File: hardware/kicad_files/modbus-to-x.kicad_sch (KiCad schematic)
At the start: 67 parts, among them IC1 ESP32-WROOM-32D_M113DH2800PH3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, J1 PWR, J2 UART, J3 Screw_Terminal_3.5mm_2, SW1 1825910-7, SW2 1825910-7, U1 AMS1117-3.3, U3 MAX3485, U5 AT24CS64-XHM, U6 AT24CS64-XHM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

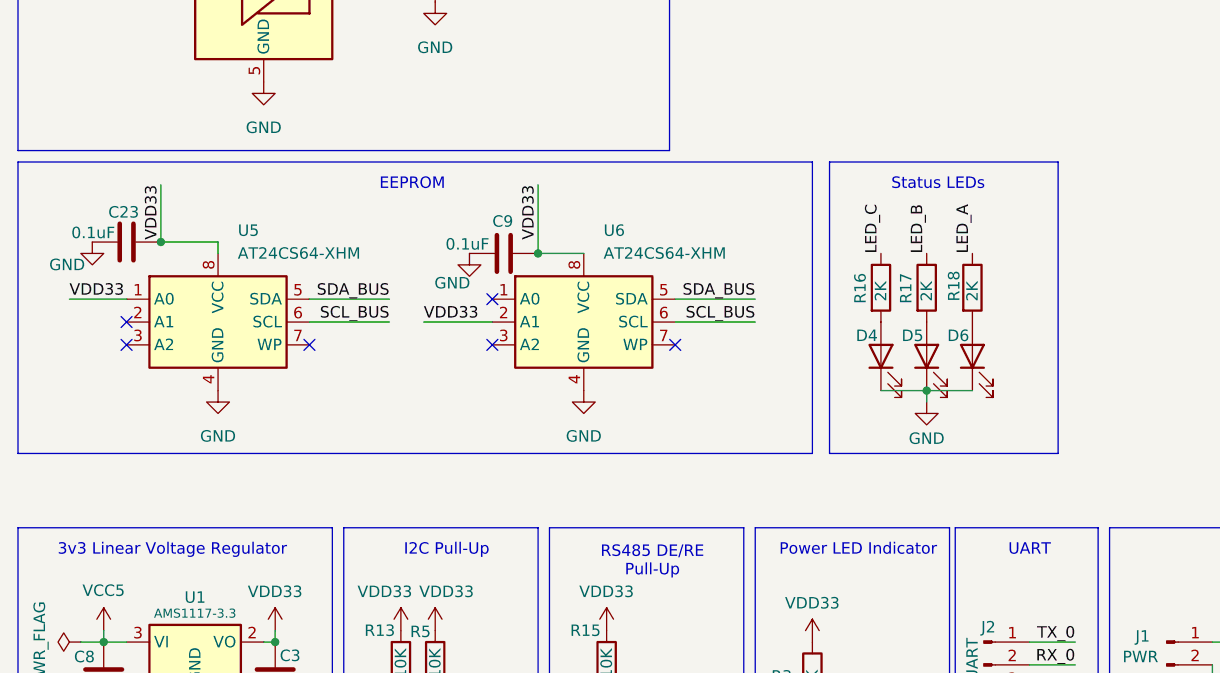
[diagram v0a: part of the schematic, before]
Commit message: refined MQTT config UI
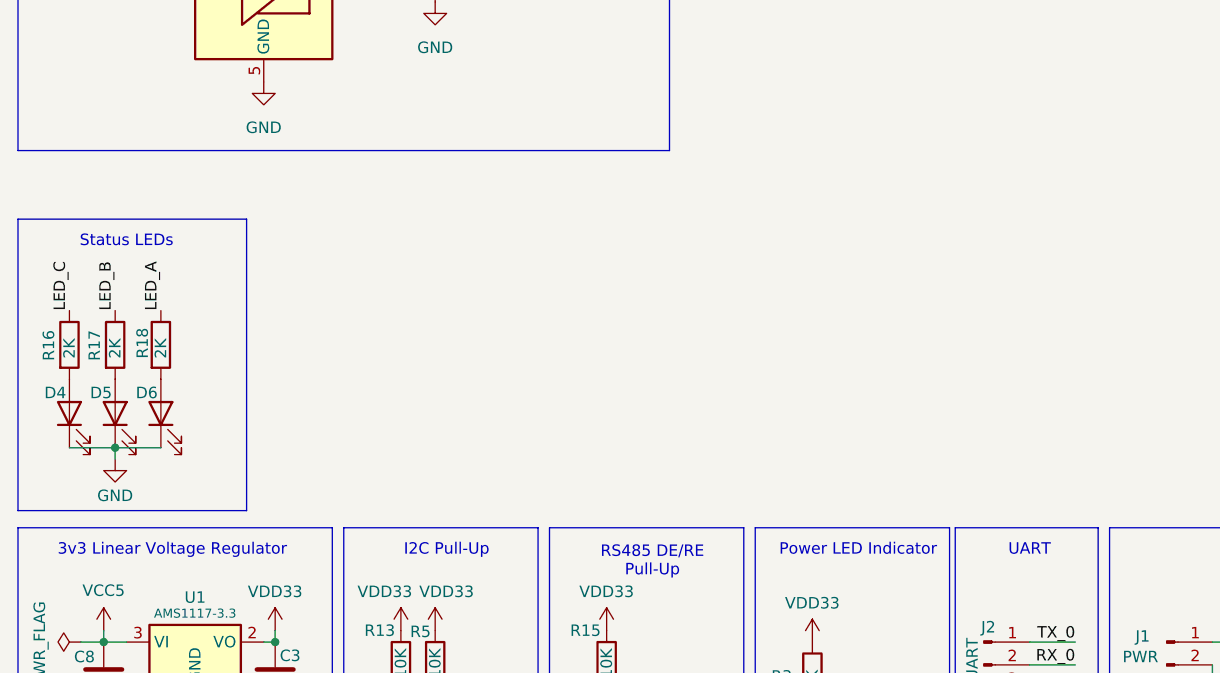
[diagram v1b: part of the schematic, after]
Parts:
- removed C23, C9: 0.1uF, Capacitor_SMD:C_1206_3216Metric_Pad1.33x1.80mm_HandSolder, symbol Device:C
- removed U5, U6: AT24CS64-XHM, Package_SO:TSSOP-8_4.4x3mm_P0.65mm, symbol Memory_EEPROM:AT24CS64-XHM
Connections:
- no-connect marks 17 -> 11
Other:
- note removed: "EEPROM"
- moved on the sheet: D4, D5, D6, R16, R17, R18

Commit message: new power circuit
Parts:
- removed C1: 47uF, Capacitor_SMD:CP_Elec_6.3x5.4, symbol Device:C_Polarized
- removed C10: 0.1uF, Capacitor_SMD:C_0805_2012Metric_Pad1.18x1.45mm_HandSolder, symbol Device:C
- removed C11, C20: 2.2nF, Capacitor_SMD:C_0805_2012Metric_Pad1.18x1.45mm_HandSolder, symbol Device:C
- removed C12, C21: 100pF, Capacitor_SMD:C_0805_2012Metric_Pad1.18x1.45mm_HandSolder, symbol Device:C
- removed C13, C14, C16, C17, C18, C2: 10uF, Capacitor_SMD:C_0805_2012Metric_Pad1.18x1.45mm_HandSolder, symbol Device:C
- removed C15, C3, C8: 22uF, Capacitor_SMD:C_0805_2012Metric_Pad1.18x1.45mm_HandSolder, symbol Device:C
- removed C19: 0.01uF, project_footprints:C_0402_1005Metric_Pad0.74x0.62mm_HandSolder_Modified_Silkscreen, symbol Device:C
- removed D2: MBRS340T3G, Diode_SMD:D_SMB-SMC_Universal_Handsoldering, symbol Diode:MBR0530
- removed FB_NODE_TP3, L1_COUT_TP6, SW_TP4, VCC5_TP5: 5029, project_footprints:KEYSTONE_5029, symbol KEYSTONE_5029:5029
- removed J1: PWR, SparkFun-Connector:Screw_Terminal_3.5mm-2, symbol Connector:Conn_01x02_Pin
- removed J2: UART, SparkFun-Connector:Screw_Terminal_3.5mm-3, symbol Connector:Conn_01x03_Pin
- removed J3: Screw_Terminal_3.5mm_2, SparkFun-Connector:Screw_Terminal_3.5mm-2, symbol SparkFun-Connector:Screw_Terminal_3.5mm_2
- removed L1: 4.7uH, WE 74404041047:L_Wurth_WE-LQS-4012, symbol SparkFun-Coil:L
- removed R10: 47k, Resistor_SMD:R_0805_2012Metric_Pad1.20x1.40mm_HandSolder, symbol Device:R
- removed R11: 22K, Resistor_SMD:R_0603_1608Metric_Pad0.98x0.95mm_HandSolder, symbol Device:R
- removed R12, R7: 620R, Resistor_SMD:R_0805_2012Metric_Pad1.20x1.40mm_HandSolder, symbol Device:R
- removed R6: 10K, Resistor_SMD:R_0805_2012Metric_Pad1.20x1.40mm_HandSolder, symbol Device:R
- removed R8: 390k, Resistor_SMD:R_0402_1005Metric_Pad0.72x0.64mm_HandSolder, symbol Device:R
- removed R9: 22k, Resistor_SMD:R_0603_1608Metric_Pad0.98x0.95mm_HandSolder, symbol Device:R
- removed U1: AMS1117-3.3, Package_TO_SOT_SMD:SOT-223-3_TabPin2, symbol Regulator_Linear:AMS1117-3.3
- removed U7: LMR14020QDPRRQ1, project_footprints:LMR14020QDPRRQ1_DPR0010A_Modified_3mm_thermals, symbol LMR14020QDPRRQ1:LMR14020QDPRRQ1
- added C23, C26: 10uF, Capacitor_SMD:C_0805_2012Metric_Pad1.18x1.45mm_HandSolder, symbol Device:C
- added C27, C28, C29: 22uF, Capacitor_SMD:C_0603_1608Metric_Pad1.08x0.95mm_HandSolder, symbol Device:C
- added C9: 0.1uF, Capacitor_SMD:C_1206_3216Metric_Pad1.33x1.80mm_HandSolder, symbol Device:C
- added J3: Screw_Terminal_3.5mm_4, SparkFun-Connector:Screw_Terminal_3.5mm-4, symbol SparkFun-Connector:Screw_Terminal_3.5mm_4
- added J4: M50-3140645R, project_footprints:HARWIN_M50-3140645R, symbol M50-3140645R:M50-3140645R
- added L2: 2uH, project_footprints:SRN8040-2R2Y, symbol Device:L
- added Q1, Q2: DSS4160U-7, project_footprints:SOT65P210X110-3N, symbol DSS4160U-7:DSS4160U-7
- added R19, R20, R22: 10K, Resistor_SMD:R_0805_2012Metric_Pad1.20x1.40mm_HandSolder, symbol Device:R
- added R21: 33.2K, Resistor_SMD:R_0805_2012Metric_Pad1.20x1.40mm_HandSolder, symbol Device:R
- added U4: TPS563208DDCT, project_footprints:TPS563208DDCT_SOT95P280X110-6N, symbol Buck Converter TPS563208DDCT:TPS563208DDCT
- added VOUT_TP1: 5029, project_footprints:KEYSTONE_5029, symbol KEYSTONE_5029:5029
- IC1: value ESP32-WROOM-32D_M113DH2800PH3Q0_ -> ESP32-WROOM-32D_M113DH2800PH3Q0; footprint project_footprints:ESP32-WROOM-32D_M113DH2800PH3Q0 -> project_footprints:ESP32-WROOM-32D_ANT_SILK_REMOVED
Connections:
- net EN: now also Q2.3 (C)
- net GND: now also C23.2, C26.1, C27.1, C28.1, C29.1, J3.4 (Pin_4), J4.1, R22.1, U4.1 (GND)
- net IO_0: now also Q1.3 (C)
- net RS485+: now also J3.2 (Pin_2)
- net RS485-: now also J3.3 (Pin_3)
- net RX_0: now also J4.2
- net TX_0: now also J4.3
- net VBUS_12: now also C23.1, C26.2, J3.1 (Pin_1), U4.3 (VIN), U4.5 (EN)
- net VDD33: now also C27.2, C28.2, C29.2, J4.6, L2.1, R21.1, VOUT_TP1.TP
- net GPIO12: no longer names the net of IC1.14 (IO12)
- net GPIO14: no longer names the net of IC1.13 (IO14)
- net GPIO27: no longer names the net of IC1.12 (IO27)
- net GPIO_34: no longer names the net of IC1.6 (IO34)
- net GPIO_35: no longer names the net of IC1.7 (IO35)
- net PGOOD: no longer names the net of IC1.16 (IO13)
- net SPI_CLK: no longer names the net of IC1.30 (IO18)
- net SPI_CS: no longer names the net of IC1.29 (IO5)
- net SPI_MISO: no longer names the net of IC1.31 (IO19)
- net SPI_MOSI: no longer names the net of IC1.37 (IO23)
- new net: R21.2, R22.2, U4.4 (VFB)
- new net: Q2.1 (B), R20.2
- new net: C9.1, L2.2, U4.2 (SW)
- new net: Q1.1 (B), R19.2
- new net: C9.2, U4.6 (VBST)
- new net DTR: J4.4, Q1.2 (E), R20.1
- new net RTS: J4.5, Q2.2 (E), R19.1
- no-connect marks 11 -> 21
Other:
- note added: "Auto Reset"
- note added: "Boot/Reset Buttons"
- note added: "Power/Data"
- note removed: "12V Input"
- note removed: "3v3 Linear Voltage Regulator"
- note removed: "Cff"
- note removed: "Cin Caps"
- note removed: "Cout Caps"
- note removed: "Css"
- note removed: "Rfbb"
- note removed: "Rt"
- note removed: "UART"
- moved on the sheet: C22, C5, C6, C7, D1, D3, R1, R13, R15, R3, R5, SW1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

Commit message: updated hw
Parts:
- removed C5, C6: 0.1uF, Capacitor_SMD:C_1206_3216Metric_Pad1.33x1.80mm_HandSolder, symbol Device:C
- removed SW1, SW2: 1825910-7, project_footprints:Switch_Tactile_SMD_6x6mm_PTS645_Modified_Silkscreen, symbol dk_Tactile-Switches:1825910-7
- added C1, C2: 0.1uF, Capacitor_SMD:C_1206_3216Metric_Pad1.33x1.80mm_HandSolder, symbol Device:C
- added SW3, SW4: 3983, project_footprints:SW_3983_ADA, symbol Adafruit 3983 Mini Soft Touch Switch:3983
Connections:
- net EN: now also C2.1, SW4.2
- net GND: now also C1.2, C2.2, SW3.1, SW4.1
- net IO_0: now also C1.1, SW3.2

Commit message: added xtal
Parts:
- added C3, C5: 12pF, Capacitor_SMD:C_0402_1005Metric_Pad0.74x0.62mm_HandSolder, symbol Device:C
- added Y1: 32.768kHz, project_footprints:XTAL_ABS05-32.768KHZ-T, symbol Device:Crystal
- J3: footprint SparkFun-Connector:Screw_Terminal_3.5mm-4 -> TerminalBlock_4Ucon:TerminalBlock_4Ucon_1x04_P3.50mm_Horizontal
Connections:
- net GND: now also C3.1, C5.1
- net LED_A: now also IC1.12 (IO27); no longer IC1.11 (IO26)
- net LED_B: now also IC1.11 (IO26); no longer IC1.10 (IO25)
- net LED_C: now also IC1.10 (IO25); no longer IC1.9 (IO33)
- net X32P: now reaches IC1.8 (IO32)
- net X32P: now also C5.2, Y1.2
- new net X32N: C3.2, IC1.9 (IO33), Y1.1
- no-connect marks 21 -> 19
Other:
- note added: "XTAL"

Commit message: bom fixes
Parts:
- added J1: 2_54mm_PinHeader1x4, Connector_PinHeader_2.54mm:PinHeader_1x04_P2.54mm_Vertical, symbol SparkFun-Connector:Screw_Terminal_3.5mm_4
- C7: PartNo CVNF100K12X -> C1206C104K5RACTU
- IC1: PartNo (none) -> M113DH2800PH3Q0
- J3: PartNo (none) -> Screw_Terminal_3.5mm_4
- J4: MANUFACTURER HARWIN -> (none); PartNo (none) -> M50-3140645R; STANDARD Manufacturer Recommendations -> (none)
- L2: PartNo (none) -> SRN8040-2R2Y
- Q1, Q2: PartNo (none) -> DSS4160U-7
- R15: value 10K -> 47K; PartNo RND 155TC0525B1002T5J -> RND 1550805S8F4702T5E
- RX2_TP1, TX2_TP2: PartNo (none) -> 5029
- SW3, SW4: PartNo (none) -> Adafruit_3983
- U3: PartNo MAX485 -> MAX3485CSA+T
- U4: MANUFACTURER Texas Instruments -> (none); MAXIMUM_PACKAGE_HEIGHT 1.10mm -> (none); PARTREV December 2015 -> (none); PartNo (none) -> TPS563208DDCT; STANDARD IPC-7351B -> (none)
- Y1: PartNo (none) -> ABS05-32.768KHZ-T
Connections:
- net GND: now also R15.1, J1.4 (Pin_4)
- net SCL_BUS: now also J1.2 (Pin_2)
- net SDA_BUS: now also J1.3 (Pin_3)
- net VDD33: now also J1.1 (Pin_1); no longer R15.1
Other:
- note added: "I2C Peripheral"
- note added: "RS485 DE/RE Pull-Down"
- note removed: "RS485 DE/RE Pull-Up"
- moved on the sheet: R15
